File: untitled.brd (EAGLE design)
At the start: 32.5 x 43 mm, 31 parts, among them SW1 SPST_TACT-KMR2, U1 ATSAMD21G-A, U2 SPX3819-3.3, U3 MCP73831T, X1 XTAL_32.768KHZ, X2 microusb

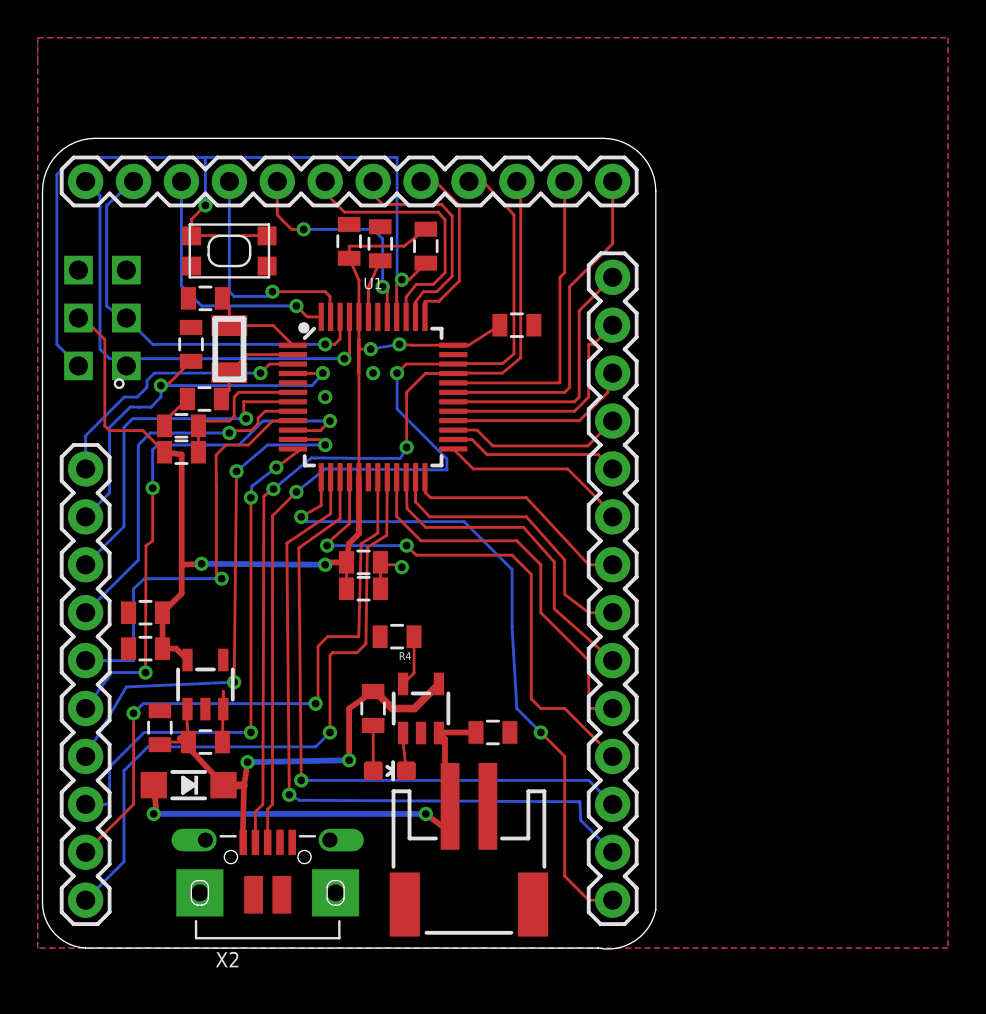
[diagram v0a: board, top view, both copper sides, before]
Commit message: update Readme and boards
Boards updated to reduce vias and moved the reset button location
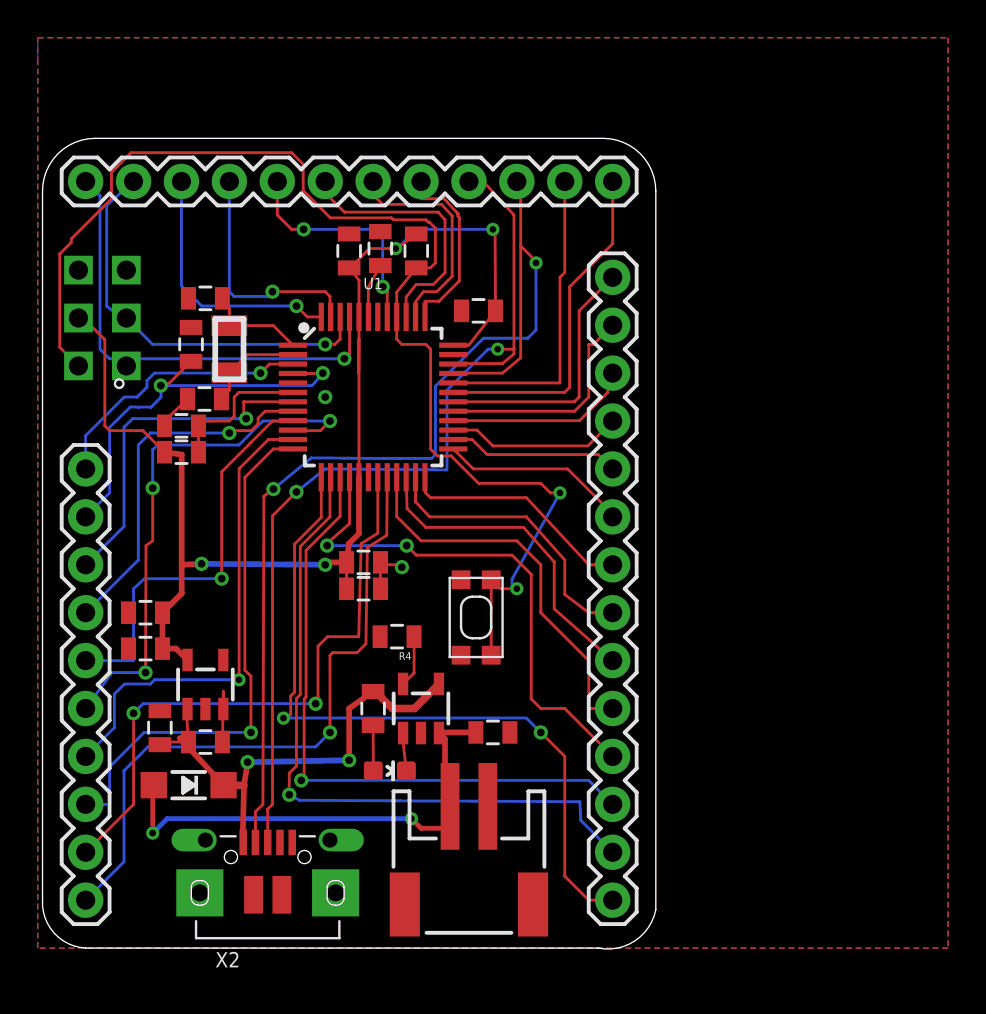
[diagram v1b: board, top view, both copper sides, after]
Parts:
- moved SW1 23.4 mm to (25.8, 22.6), turned to 270 degrees
- moved C4 2.17 mm to (25.9, 38.9), turned to 180 degrees
- moved R1 0.57 mm to (22.6, 42.0)
- moved C5 0.51 mm to (19.1, 42.0)
- moved C6 0.25 mm to (20.7, 42.2)
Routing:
- net RESET: track 48.0 -> 65.7 mm
- net D-: track 46.2 -> 56.9 mm
- net 3.3V: track 64.9 -> 69.3 mm
- net PA08: track 35.4 -> 38.9 mm
- net PA06: track 28.2 -> 25.5 mm, vias 3 -> 1
- net V_BATT: track 24.8 -> 26.1 mm
- net PA04: track 22.7 -> 21.8 mm
- net D+: track 51.0 -> 50.3 mm
- net PA07: track 28.3 -> 28.8 mm, vias 3 -> 1
- net GND: track 4.40 -> 4.34 mm, vias 3 -> 2
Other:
- board text added: "WestSideElectronics M0 Plus Board v1.2 2 AUG 2017"
- board text removed: "WestSideElectronics M0 Plus Board v1.1 2 MAY 2017"
